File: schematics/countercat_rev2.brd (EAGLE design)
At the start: 101.6 x 76.2 mm, 67 parts, among them Q1 IRF520, Q2 2N3904, Q3 IRF520, Q4 IRF520, Q5 IRF520, U4 ATMEGA328P_PDIP, U6 RELAYPTH3, Y1 16MHz

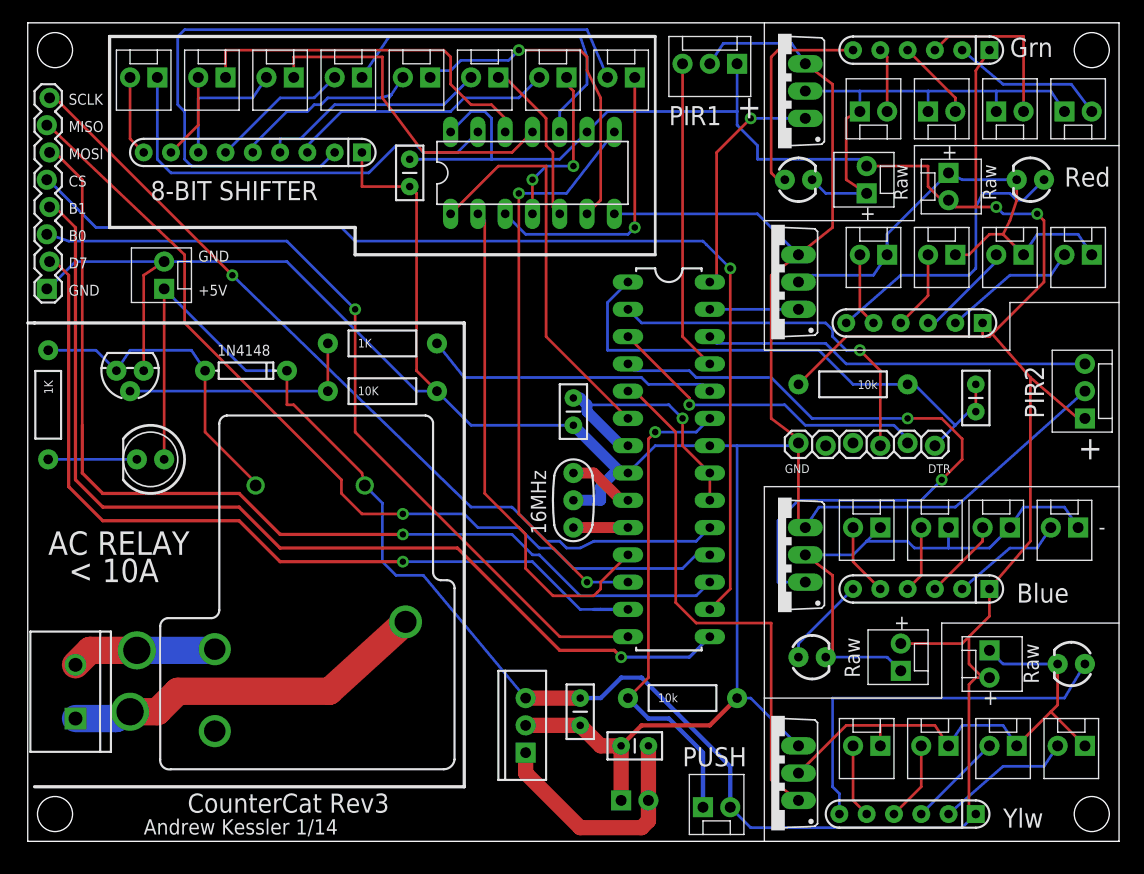
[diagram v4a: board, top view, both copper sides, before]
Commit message: Got rid of relay on board. Made smaller, swapepd out shift reg. for decoder
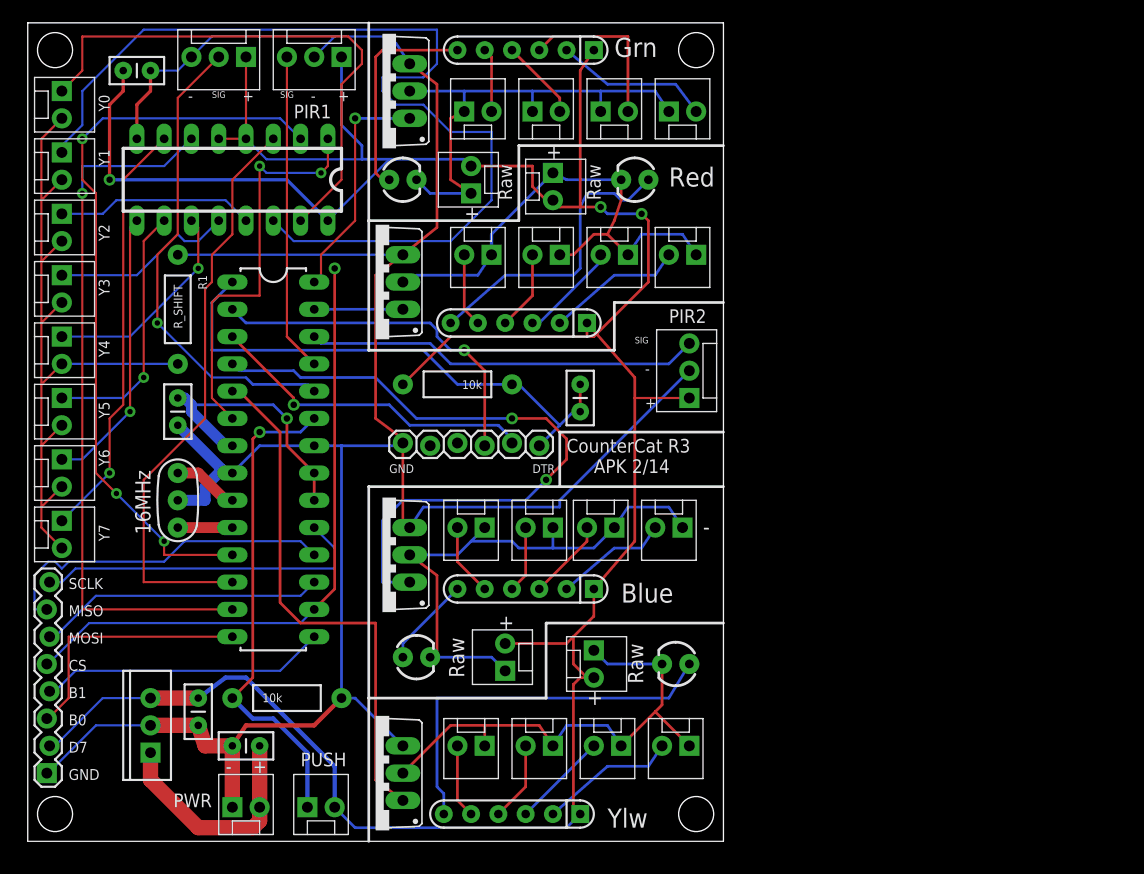
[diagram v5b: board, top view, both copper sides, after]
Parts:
- removed C6: .1uF, SparkFun-Capacitors:CAP-PTH-SMALL2
- removed D1: 1N4148, SparkFun:DIODE-1N4148
- removed JP36: AUX_PWR, SparkFun:MOLEX-1X2
- removed LED1: (no value), SparkFun:LED5MM
- removed Q2: 2N3904, SparkFun:TO-92
- removed R11: R-SHF, SparkFun-Resistors:RPACK-SIP-PTH-8
- removed R3: 10K, SparkFun-Resistors:AXIAL-0.4
- removed R4: 1K, SparkFun-Resistors:AXIAL-0.4
- removed U$15: 74XX164, andrews_eagle_lib:DIP14
- removed U6: RELAYPTH3, SparkFun:RELAY-T9A-2
- added C4: .1uF, SparkFun-Capacitors:CAP-PTH-SMALL2
- added U$7: M74HC238, SparkFun-DigitalIC:DIL16
- JP15: value Load -> RELAY; device SparkFun:SCREWTERMINAL-5MM-2 -> SparkFun:MOLEX-1X3
- R1: value 1K -> R_SHIFT
- U4: value ATMEGA328P_PDIP -> ATMEGA328P
- moved JP15 63.6 mm to (20.3, 73.0), turned to 180 degrees
- moved JP18 53.4 mm to (3.17, 69.8), turned to 270 degrees
- moved JP19 47.5 mm to (3.17, 64.1), turned to 270 degrees
- moved JP35 45.1 mm to (1.91, 6.35)
- moved JP16 42.6 mm to (3.17, 58.4), turned to 270 degrees
- moved JP20 42.2 mm to (3.17, 29.8), turned to 270 degrees
- moved JP2 38.9 mm to (3.17, 52.7), turned to 270 degrees
- moved JP21 38.7 mm to (3.17, 35.6), turned to 270 degrees
- moved JP17 36.9 mm to (3.17, 47.0), turned to 270 degrees
- moved JP5 36.9 mm to (61.6, 41.3)
- moved JP1 36.8 mm to (29.2, 73.0)
- moved JP22 36.8 mm to (3.17, 41.3), turned to 270 degrees
- moved BLU 36.8 mm to (36.2, 17.1)
- moved JP24 36.8 mm to (41.3, 60.3)
- moved JP25 36.8 mm to (61.0, 29.2)
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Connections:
- removed net COIL: D1.A, Q2.3, R4.P$1, U6.COIL2
- removed net D7: JP35.2, U4.13
- removed net DSA: U$15.1, U4.6
- removed net DSB: U$15.2, U4.11
- removed net LOAD1: JP15.1, U6.MAIN
- removed net LOAD2: JP15.2, U6.NO
- removed net N$10: JP18.2, R11.P$2
- removed net N$11: JP19.2, R11.P$3
- removed net N$14: JP16.2, R11.P$4
- removed net N$17: JP2.2, R11.P$5
- removed net N$20: JP17.2, R11.P$6
- removed net N$23: JP22.2, R11.P$7
- removed net N$24: JP21.2, R11.P$8
- removed net N$6: Q2.2, R1.P$1, R3.P$1
- removed net N$9: LED1.K, R4.P$2
- removed net SRCLK: U$15.8, U4.12
- new net D_A: U$7.1, U4.6
- new net D_B: U$7.2, U4.11
- new net D_C: U$7.3, U4.12
- new net D_EN: U$7.6, U4.13
- net 5V: now also C4.1, JP15.1, JP35.2, U$7.16, U$7.4, U$7.5; no longer C6.2, D1.C, JP36.1, LED1.A, U$15.14, U$15.9, U6.COIL1
- net GND: now also C4.2, JP15.3, R1.P$1, U$7.8; no longer C6.1, JP36.2, Q2.1, R11.P$1, R3.P$2, U$15.7
- net N$1: now also U$7.11; no longer U$15.10
- net N$25: now also JP16.2, JP17.2, JP18.2, JP19.2, JP2.2, JP21.2, JP22.2, R1.P$2; no longer R11.P$9
- net N$26: now also U$7.15; no longer U$15.3
- net N$27: now also U$7.14; no longer U$15.4
- net N$28: now also U$7.13; no longer U$15.5
- net N$29: now also U$7.12; no longer U$15.6
- net N$30: now also U$7.9; no longer U$15.12
- net N$31: now also U$7.10; no longer U$15.11
- net N$32: now also U$7.7; no longer U$15.13
- net RELAY: now also JP15.2; no longer R1.P$2
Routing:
- net D7: track 79.4 -> 0.00 mm, vias 1 -> 0
- net N$27: track 16.0 -> 92.7 mm, vias 2 -> 0
- net D_B: track 0.00 -> 70.1 mm, vias 0 -> 3
- net N$10: track 69.7 -> 0.00 mm
- net SPI_MOSI: track 95.1 -> 26.7 mm, vias 1 -> 0
- net B1: track 93.4 -> 26.7 mm, vias 1 -> 0
- net D_EN: track 0.00 -> 66.5 mm, vias 0 -> 1
- net N$25: track 7.51 -> 68.5 mm
- net GND: track 293.5 -> 238.4 mm
- net D_C: track 0.00 -> 54.5 mm
- net SRCLK: track 54.3 -> 0.00 mm, vias 2 -> 0
- net B0: track 76.2 -> 23.8 mm, vias 1 -> 0
- net SPI_MISO: track 83.6 -> 32.7 mm, vias 1 -> 0
- net SPI_SCK: track 79.3 -> 31.7 mm, vias 1 -> 0
- net DSB: track 47.4 -> 0.00 mm
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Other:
- board size 101.6 x 76.2 mm -> 64.8 x 76.2 mm
- board text added: "APK 2/14"
- board text added: "CounterCat R3"
- board text added: "PWR"
- board text added: "RELAY"
- board text added: "SIG"
- board text added: "Y0"
- board text added: "Y1"
- board text added: "Y2"
- board text added: "Y3"
- board text added: "Y4"
- board text added: "Y5"
- board text added: "Y6"
- board text added: "Y7"
- board text removed: "+5V"
- board text removed: "8-BIT SHIFTER"
- board text removed: "< 10A"
- board text removed: "AC RELAY"
- board text removed: "Andrew Kessler 1/14"
- board text removed: "CounterCat Rev3"

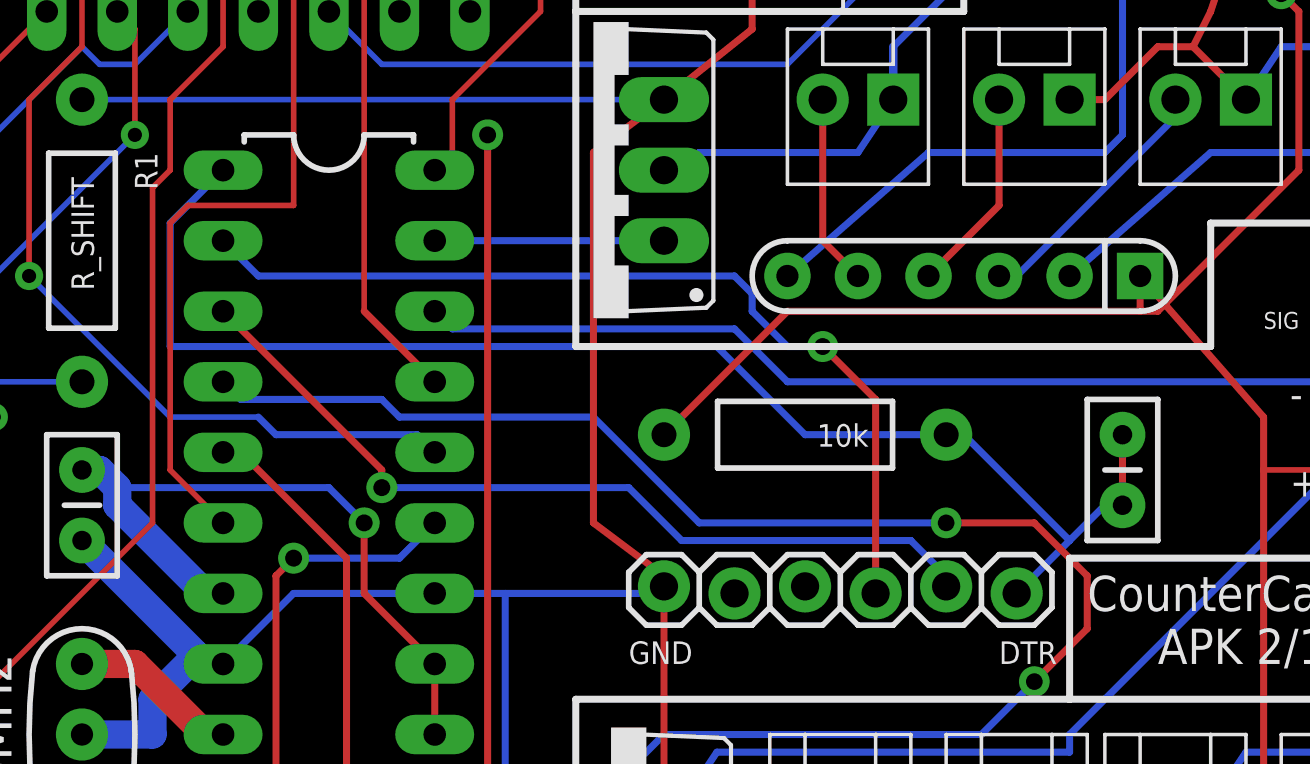
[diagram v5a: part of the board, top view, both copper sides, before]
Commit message: Fixed error with shorted DTR net in schematic
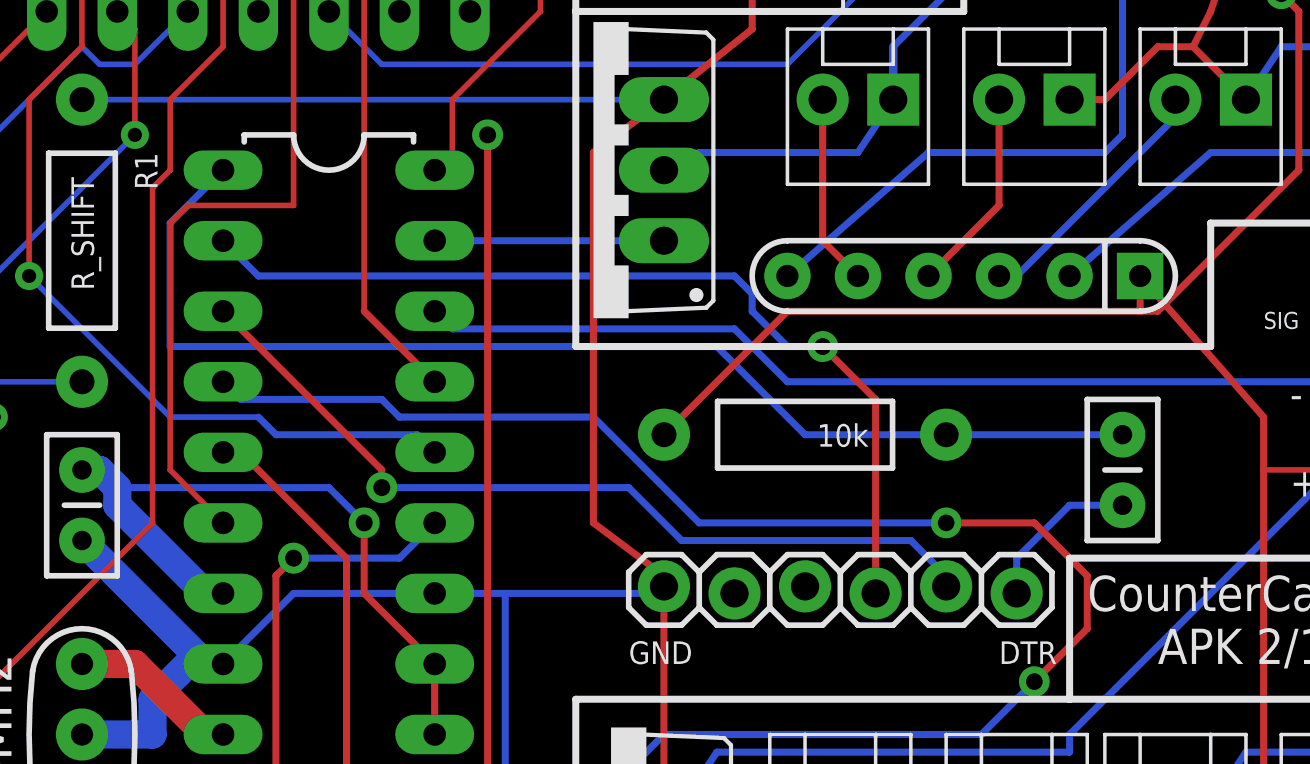
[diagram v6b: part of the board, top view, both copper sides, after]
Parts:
- moved C2 2.54 mm to (51.4, 40.0), turned to 90 degrees
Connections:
- new net RES: C2.2, R7.P$1, U4.1
- net DTR: no longer C2.2, R7.P$1, U4.1
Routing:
- net DTR: track 50.1 -> 5.87 mm
- net RES: track 0.00 -> 42.7 mm
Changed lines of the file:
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@@
 </element>
 <element name="Y1" library="SparkFun-FreqCtrl" package="RESONATOR-PTH" value="16MHz" x="13.97" y="31.75" rot="R270"/>
-<element name="C2" library="SparkFun-Capacitors" package="CAP-PTH-SMALL2" value=".1uF" x="51.435" y="42.545" smashed="yes" rot="R270"/>
+<element name="C2" library="SparkFun-Capacitors" package="CAP-PTH-SMALL2" value=".1uF" x="51.435" y="40.005" smashed="yes" rot="R90"/>
 <element name="R7" library="SparkFun-Resistors" package="AXIAL-0.4" value="10k" x="40.005" y="42.545" smashed="yes" rot="R180">
 <attribute name="VALUE" x="42.291" y="42.926" size="0.8128" layer="21" font="vector" ratio="15" rot="R180"/>
@@
 </signal>
 <signal name="DTR">
-<contactref element="C2" pad="2"/>
-<contactref element="R7" pad="P$1"/>
-<contactref element="U4" pad="1"/>
+<contactref element="JP6" pad="1"/>
 <contactref element="C2" pad="1"/>
-<contactref element="JP6" pad="1"/>
-<wire x1="51.435" y1="42.545" x2="51.435" y2="40.005" width="0.254" layer="1"/>
-<wire x1="50.8" y1="40.005" x2="49.53" y2="38.735" width="0.254" layer="16"/>
-<wire x1="49.53" y1="38.735" x2="47.625" y2="36.83" width="0.254" layer="16"/>
-<wire x1="51.435" y1="40.005" x2="50.8" y2="40.005" width="0.254" layer="16"/>
-<wire x1="17.145" y1="50.165" x2="19.05" y2="52.07" width="0.254" layer="16"/>
-<wire x1="17.145" y1="45.72" x2="17.145" y2="50.165" width="0.254" layer="16"/>
-<wire x1="36.83" y1="45.72" x2="17.145" y2="45.72" width="0.254" layer="16"/>
-<wire x1="40.005" y1="42.545" x2="36.83" y2="45.72" width="0.254" layer="16"/>
-<wire x1="45.085" y1="42.545" x2="40.005" y2="42.545" width="0.254" layer="16"/>
-<wire x1="45.72" y1="42.545" x2="49.53" y2="38.735" width="0.254" layer="16"/>
-<wire x1="45.085" y1="42.545" x2="45.72" y2="42.545" width="0.254" layer="16"/>
+<wire x1="47.625" y1="36.83" x2="47.625" y2="38.1" width="0.254" layer="16"/>
+<wire x1="47.625" y1="38.1" x2="49.53" y2="40.005" width="0.254" layer="16"/>
+<wire x1="49.53" y1="40.005" x2="51.435" y2="40.005" width="0.254" layer="16"/>
 </signal>
 <signal name="N$3">
@@
 <via x="5.08" y="60.325" extent="1-16" drill="0.508"/>
 </signal>
+<signal name="RES">
+<contactref element="C2" pad="2"/>
+<contactref element="R7" pad="P$1"/>
+<contactref element="U4" pad="1"/>
+<wire x1="17.145" y1="45.72" x2="17.145" y2="50.165" width="0.254" layer="16"/>
+<wire x1="36.83" y1="45.72" x2="17.145" y2="45.72" width="0.254" layer="16"/>
+<wire x1="40.005" y1="42.545" x2="36.83" y2="45.72" width="0.254" layer="16"/>
+<wire x1="45.085" y1="42.545" x2="40.005" y2="42.545" width="0.254" layer="16"/>
+<wire x1="45.085" y1="42.545" x2="51.435" y2="42.545" width="0.254" layer="16"/>
+<wire x1="19.05" y1="52.07" x2="17.145" y2="50.165" width="0.254" layer="16"/>
+</signal>
 </signals>
